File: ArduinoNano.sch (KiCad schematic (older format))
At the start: 14 parts, among them IC801 ATMEGA328P-AU, IC802 FT232RL-TUBE, J801 M20-9980345, J802 USB_Connector, Y801 Crystal

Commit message: finalized nano (references, one more resistor...)
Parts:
- removed R199: 146, symbol Device:R
- added RP1D801, RP2C801: 1k, symbol Device:R
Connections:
- net +5V: now also RP1D801.1
- net GND: now also RP2C801.1, RP2C801.2
- net RESET: now also IC801.29 (PC6_[RESET/PCINT14]), RP1D801.2
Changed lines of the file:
@@
 U 1 1 60D08921
 P 2850 1900
-F 0 "RP1B801" H 2600 2050 50  0000 L CNN
+F 0 "RP1B801" H 2500 2050 50  0000 L CNN
 F 1 "1k" H 2600 1950 50  0000 L CNN
 F 2 "" V 2780 1900 50  0001 C CNN
@@
 U 1 1 60D0986A
 P 3100 1900
-F 0 "RP1A801" H 3100 2050 50  0000 L CNN
-F 1 "1k" H 3200 1950 50  0000 L CNN
+F 0 "RP1A801" H 2750 2150 50  0000 L CNN
+F 1 "1k" H 2950 2050 50  0000 L CNN
 F 2 "" V 3030 1900 50  0001 C CNN
 F 3 "~" H 3100 1900 50  0001 C CNN
@@
 U 1 1 60D5814C
 P 1200 5200
-F 0 "C803" H 1315 5246 50  0000 L CNN
-F 1 "1uf" H 1315 5155 50  0000 L CNN
+F 0 "C803" H 900 5300 50  0000 L CNN
+F 1 "1uf" H 950 5200 50  0000 L CNN
 F 2 "" H 1238 5050 50  0001 C CNN
 F 3 "~" H 1200 5200 50  0001 C CNN
@@
 U 1 1 60D58539
 P 1900 5200
-F 0 "C805" H 2015 5246 50  0000 L CNN
+F 0 "C805" H 2000 5250 50  0000 L CNN
 F 1 "1uf" H 2015 5155 50  0000 L CNN
 F 2 "" H 1938 5050 50  0001 C CNN
@@
 U 1 1 60D58EE5
 P 1550 5200
-F 0 "C804" H 1668 5246 50  0000 L CNN
-F 1 "4.7uF_16V" H 1450 5350 50  0000 L CNN
+F 0 "C804" H 1350 5100 50  0000 L CNN
+F 1 "4.7uF_16V" H 1350 5000 50  0000 L CNN
 F 2 "" H 1588 5050 50  0001 C CNN
 F 3 "~" H 1550 5200 50  0001 C CNN
@@
 U 1 1 60D9EF9C
 P 1050 4100
-F 0 "C801" V 900 4100 50  0000 C CNN
+F 0 "C801" V 900 4050 50  0000 C CNN
 F 1 "C" V 900 4200 50  0000 C CNN
 F 2 "" H 1088 3950 50  0001 C CNN
@@
 U 1 1 60DA0A1E
 P 1050 4400
-F 0 "C802" V 1200 4400 50  0000 C CNN
+F 0 "C802" V 1200 4350 50  0000 C CNN
 F 1 "C" V 1200 4500 50  0000 C CNN
 F 2 "" H 1088 4250 50  0001 C CNN
@@
 Wire Wire Line
 	6200 5800 5650 5800
-$Comp
-L Device:R R199
-U 1 1 60CC8A37
-P 7200 2300
-F 0 "R199" H 7270 2346 50  0000 L CNN
-F 1 "146" H 7270 2255 50  0000 L CNN
-F 2 "" V 7130 2300 50  0001 C CNN
-F 3 "~" H 7200 2300 50  0001 C CNN
-	1    7200 2300
-	1    0    0    -1
-$EndComp
+Wire Wire Line
+	3350 1800 3350 2200
+Wire Wire Line
+	3350 1800 3850 1800
+Wire Wire Line
+	3850 1800 3850 1700
+$Comp
+L Device:R RP1D801
+U 1 1 60CE678B
+P 3850 1550
+F 0 "RP1D801" H 3920 1596 50  0000 L CNN
+F 1 "1k" H 3920 1505 50  0000 L CNN
+F 2 "" V 3780 1550 50  0001 C CNN
+F 3 "~" H 3850 1550 50  0001 C CNN
+	1    3850 1550
+	1    0    0    -1
+$EndComp
+$Comp
+L power:+5V #PWR0813
+U 1 1 60CE727D
+P 3850 1400
+F 0 "#PWR0813" H 3850 1250 50  0001 C CNN
+F 1 "+5V" H 3865 1573 50  0000 C CNN
+F 2 "" H 3850 1400 50  0001 C CNN
+F 3 "" H 3850 1400 50  0001 C CNN
+	1    3850 1400
+	1    0    0    -1
+$EndComp
+Text Label 3450 1800 0    50   ~ 0
+RESET
+$Comp
+L Device:R RP2C801
+U 1 1 60CEA708
+P 5550 3100
+F 0 "RP2C801" V 5343 3100 50  0000 C CNN
+F 1 "1k" V 5434 3100 50  0000 C CNN
+F 2 "" V 5480 3100 50  0001 C CNN
+F 3 "~" H 5550 3100 50  0001 C CNN
+	1    5550 3100
+	0    1    1    0
+$EndComp
+Wire Wire Line
+	5700 3100 5700 3250
+Wire Wire Line
+	5700 3250 5400 3250
+Wire Wire Line
+	5400 3250 5400 3100
+Wire Wire Line
+	5400 3250 5400 3350
+Connection ~ 5400 3250
+$Comp
+L power:GND #PWR0814
+U 1 1 60CF0B8E
+P 5400 3350
+F 0 "#PWR0814" H 5400 3100 50  0001 C CNN
+F 1 "GND" H 5405 3177 50  0000 C CNN
+F 2 "" H 5400 3350 50  0001 C CNN
+F 3 "" H 5400 3350 50  0001 C CNN
+	1    5400 3350
+	1    0    0    -1
+$EndComp

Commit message: add footprints julia
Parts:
- IC802: footprint SOP65P780X200-28N -> footprint libraries:FT232RL-TUBE
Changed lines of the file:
@@
 F 0 "IC802" H 8500 4315 50  0000 C CNN
 F 1 "FT232RL-TUBE" H 8500 4224 50  0000 C CNN
-F 2 "SOP65P780X200-28N" H 9000 4150 50  0001 L CNN
+F 2 "footprint libraries:FT232RL-TUBE" H 9000 4150 50  0001 L CNN
 F 3 "http://www.ftdichip.com/Support/Documents/DataSheets/ICs/DS_FT232R.pdf" H 9000 4050 50  0001 L CNN
 F 4 "USB Interface IC FT232R Single Ch Full Speed" H 9000 3950 50  0001 L CNN "Description"

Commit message: add footprints 2 julia
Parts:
- IC801: footprint QFP80P900X900X120-32N -> footprint libraries:QFP80P900X900X120-32N
- J801: footprint HDRV6W64P254_2X3_762X508X864P -> footprint libraries:M20-9980345
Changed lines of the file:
@@
 F 0 "IC801" H 3400 3300 50  0000 L CNN
 F 1 "ATMEGA328P-AU" H 3150 3200 50  0000 L CNN
-F 2 "QFP80P900X900X120-32N" H 4300 4800 50  0001 L CNN
+F 2 "footprint libraries:QFP80P900X900X120-32N" H 4300 4800 50  0001 L CNN
 F 3 "https://componentsearchengine.com/Datasheets/2/ATMEGA328P-AU.pdf" H 4300 4700 50  0001 L CNN
 F 4 "MICROCHIP - ATMEGA328P-AU. - MICROCONTROLLER MCU, 8 BIT, ATMEGA, 20MHZ, TQFP-32" H 4300 4600 50  0001 L CNN "Description"
@@
 F 0 "J801" H 6600 5865 50  0000 C CNN
 F 1 "M20-9980345" H 6600 5774 50  0000 C CNN
-F 2 "HDRV6W64P254_2X3_762X508X864P" H 6850 5700 50  0001 L CNN
+F 2 "footprint libraries:M20-9980345" H 6850 5700 50  0001 L CNN
 F 3 "https://componentsearchengine.com/Datasheets/2/M20-9980345.pdf" H 6850 5600 50  0001 L CNN
 F 4 "M20 Header, Pin, Dil, Vertical, 3+3 W HARWIN M20 Series, 2.54mm Pitch 6 Way 2 Row Straight Pin Header, Through Hole, Solder Termination" H 6850 5500 50  0001 L CNN "Description"

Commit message: added vishay dude & capacitor & resistor footprints
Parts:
- C801, C802, C803, C804, C805, C806: footprint (none) -> Capacitor_SMD:C_0402_1005Metric
- J802: footprint (none) -> footprint libraries:UX60MB5ST
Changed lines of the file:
@@
 F 0 "C806" H 5315 4346 50  0000 L CNN
 F 1 "100nF" H 5315 4255 50  0000 L CNN
-F 2 "" H 5238 4150 50  0001 C CNN
+F 2 "Capacitor_SMD:C_0402_1005Metric" H 5238 4150 50  0001 C CNN
 F 3 "~" H 5200 4300 50  0001 C CNN
 	1    5200 4300
@@
 F 0 "C803" H 900 5300 50  0000 L CNN
 F 1 "1uf" H 950 5200 50  0000 L CNN
-F 2 "" H 1238 5050 50  0001 C CNN
+F 2 "Capacitor_SMD:C_0402_1005Metric" H 1238 5050 50  0001 C CNN
 F 3 "~" H 1200 5200 50  0001 C CNN
 	1    1200 5200
@@
 F 0 "C805" H 2000 5250 50  0000 L CNN
 F 1 "1uf" H 2015 5155 50  0000 L CNN
-F 2 "" H 1938 5050 50  0001 C CNN
+F 2 "Capacitor_SMD:C_0402_1005Metric" H 1938 5050 50  0001 C CNN
 F 3 "~" H 1900 5200 50  0001 C CNN
 	1    1900 5200
@@
 F 0 "C804" H 1350 5100 50  0000 L CNN
 F 1 "4.7uF_16V" H 1350 5000 50  0000 L CNN
-F 2 "" H 1588 5050 50  0001 C CNN
+F 2 "Capacitor_SMD:C_0402_1005Metric" H 1588 5050 50  0001 C CNN
 F 3 "~" H 1550 5200 50  0001 C CNN
 	1    1550 5200
@@
 F 0 "C801" V 900 4050 50  0000 C CNN
 F 1 "C" V 900 4200 50  0000 C CNN
-F 2 "" H 1088 3950 50  0001 C CNN
+F 2 "Capacitor_SMD:C_0402_1005Metric" H 1088 3950 50  0001 C CNN
 F 3 "~" H 1050 4100 50  0001 C CNN
 	1    1050 4100
@@
 F 0 "C802" V 1200 4350 50  0000 C CNN
 F 1 "C" V 1200 4500 50  0000 C CNN
-F 2 "" H 1088 4250 50  0001 C CNN
+F 2 "Capacitor_SMD:C_0402_1005Metric" H 1088 4250 50  0001 C CNN
 F 3 "~" H 1050 4400 50  0001 C CNN
 	1    1050 4400
@@
 F 0 "J802" H 10400 5815 50  0000 C CNN
 F 1 "USB_Connector" H 10400 5724 50  0000 C CNN
-F 2 "" H 10400 5350 50  0001 C CNN
+F 2 "footprint libraries:UX60MB5ST" H 10400 5350 50  0001 C CNN
 F 3 "" H 10400 5350 50  0001 C CNN
 	1    10400 5350

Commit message: added osciallator libs
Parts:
- RP1A801, RP1B801, RP1D801, RP2C801: footprint (none) -> Resistor_SMD:R_0402_1005Metric
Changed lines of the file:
@@
 F 0 "RP1B801" H 2500 2050 50  0000 L CNN
 F 1 "1k" H 2600 1950 50  0000 L CNN
-F 2 "" V 2780 1900 50  0001 C CNN
+F 2 "Resistor_SMD:R_0402_1005Metric" V 2780 1900 50  0001 C CNN
 F 3 "~" H 2850 1900 50  0001 C CNN
 	1    2850 1900
@@
 F 0 "RP1A801" H 2750 2150 50  0000 L CNN
 F 1 "1k" H 2950 2050 50  0000 L CNN
-F 2 "" V 3030 1900 50  0001 C CNN
+F 2 "Resistor_SMD:R_0402_1005Metric" V 3030 1900 50  0001 C CNN
 F 3 "~" H 3100 1900 50  0001 C CNN
 	1    3100 1900
@@
 F 0 "RP1D801" H 3920 1596 50  0000 L CNN
 F 1 "1k" H 3920 1505 50  0000 L CNN
-F 2 "" V 3780 1550 50  0001 C CNN
+F 2 "Resistor_SMD:R_0402_1005Metric" V 3780 1550 50  0001 C CNN
 F 3 "~" H 3850 1550 50  0001 C CNN
 	1    3850 1550
@@
 F 0 "RP2C801" V 5343 3100 50  0000 C CNN
 F 1 "1k" V 5434 3100 50  0000 C CNN
-F 2 "" V 5480 3100 50  0001 C CNN
+F 2 "Resistor_SMD:R_0402_1005Metric" V 5480 3100 50  0001 C CNN
 F 3 "~" H 5550 3100 50  0001 C CNN
 	1    5550 3100

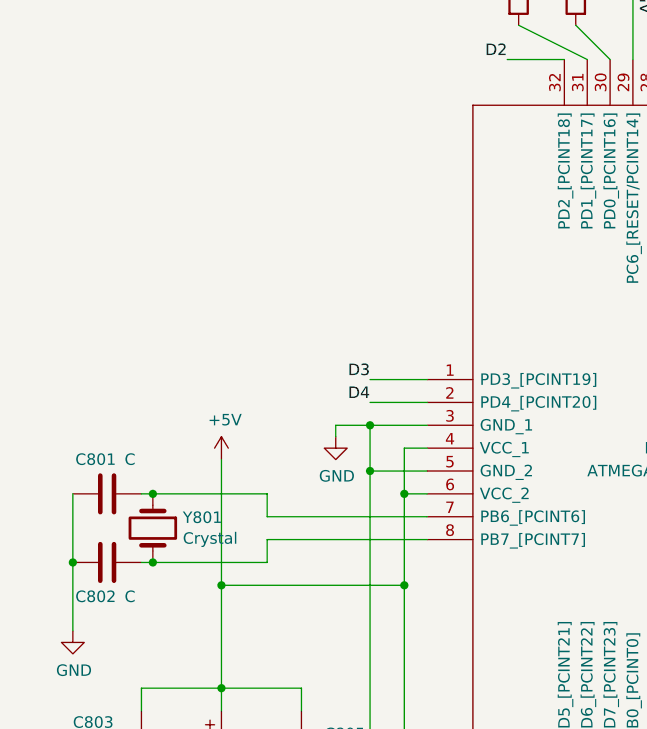
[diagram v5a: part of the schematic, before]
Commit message: replace crystal
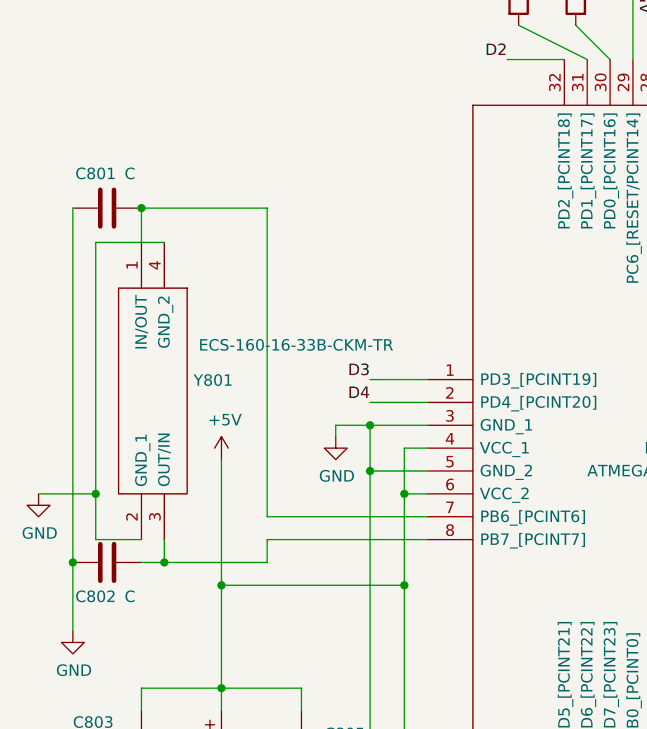
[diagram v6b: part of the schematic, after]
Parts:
- removed Y801: Crystal, symbol Device:Crystal
- added Y801: ECS-160-16-33B-CKM-TR, footprint libraries:ECS1601633BCKMTR, symbol ECS-160-16-33B-CKM-TR:ECS-160-16-33B-CKM-TR
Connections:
- net GND: now also Y801.2 (GND_1), Y801.4 (GND_2)
- net at C801.1, IC801.7 (PB6_[PCINT6]): now also Y801.1 (IN/OUT)
- net at C802.1, IC801.8 (PB7_[PCINT7]): now also Y801.3 (OUT/IN)
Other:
- moved on the sheet: C801
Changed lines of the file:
@@
 	1550 4500 1550 4950
 Connection ~ 1550 4500
-$Comp
-L Device:Crystal Y801
-U 1 1 60D95420
-P 1250 4250
-F 0 "Y801" V 1204 4381 50  0000 L CNN
-F 1 "Crystal" V 1295 4381 50  0000 L CNN
-F 2 "" H 1250 4250 50  0001 C CNN
-F 3 "~" H 1250 4250 50  0001 C CNN
-	1    1250 4250
-	0    1    1    0
-$EndComp
-Wire Wire Line
-	1750 4200 1750 4100
-Wire Wire Line
-	1750 4100 1250 4100
-Connection ~ 1250 4100
 Wire Wire Line
 	1750 4300 1750 4400
-Wire Wire Line
-	1750 4400 1250 4400
 $Comp
 L Device:C C801
 U 1 1 60D9EF9C
-P 1050 4100
-F 0 "C801" V 900 4050 50  0000 C CNN
-F 1 "C" V 900 4200 50  0000 C CNN
-F 2 "Capacitor_SMD:C_0402_1005Metric" H 1088 3950 50  0001 C CNN
-F 3 "~" H 1050 4100 50  0001 C CNN
-	1    1050 4100
-	0    1    1    0
-$EndComp
-Wire Wire Line
-	1250 4100 1200 4100
+P 1050 2850
+F 0 "C801" V 900 2800 50  0000 C CNN
+F 1 "C" V 900 2950 50  0000 C CNN
+F 2 "Capacitor_SMD:C_0402_1005Metric" H 1088 2700 50  0001 C CNN
+F 3 "~" H 1050 2850 50  0001 C CNN
+	1    1050 2850
+	0    1    1    0
+$EndComp
 $Comp
 L Device:C C802
@@
 	0    1    1    0
 $EndComp
-Connection ~ 1250 4400
-Wire Wire Line
-	1200 4400 1250 4400
-Wire Wire Line
-	900  4100 900  4400
 Connection ~ 900  4400
 Wire Wire Line
@@
 	1    0    0    -1
 $EndComp
+$Comp
+L ECS-160-16-33B-CKM-TR:ECS-160-16-33B-CKM-TR Y801
+U 1 1 60CE517B
+P 1300 3000
+F 0 "Y801" V 1904 3128 50  0000 L CNN
+F 1 "ECS-160-16-33B-CKM-TR" V 1750 3150 50  0000 L CNN
+F 2 "footprint libraries:ECS1601633BCKMTR" H 2450 3100 50  0001 L CNN
+F 3 "" H 2450 3000 50  0001 L CNN
+F 4 "Crystals CRYSTAL 16.000MHZ 16PF SMD,ECS-33B,+/-10ppm,+/-10ppm,60 Ohm,Fundamental,-20 C 70 C,4-SMD, No Lead (DFN, LCC),0.126\" L x 0.098\" W (3.20mm x 2.50mm),0.031\" (0.80mm)" H 2450 2900 50  0001 L CNN "Description"
+F 5 "0.8" H 2450 2800 50  0001 L CNN "Height"
+F 6 "520-160-16-33B-CKMTR" H 2450 2700 50  0001 L CNN "Mouser Part Number"
+F 7 "https://www.mouser.co.uk/ProductDetail/ECS/ECS-160-16-33B-CKM-TR/?qs=W%2FMpXkg%252BdQ6JQ%2Fy9oiIGzw%3D%3D" H 2450 2600 50  0001 L CNN "Mouser Price/Stock"
+F 8 "ECS" H 2450 2500 50  0001 L CNN "Manufacturer_Name"
+F 9 "ECS-160-16-33B-CKM-TR" H 2450 2400 50  0001 L CNN "Manufacturer_Part_Number"
+	1    1300 3000
+	0    1    1    0
+$EndComp
+Wire Wire Line
+	1200 2850 1750 2850
+Wire Wire Line
+	1200 4400 1300 4400
+Wire Wire Line
+	1200 3000 1200 2850
+Connection ~ 1200 2850
+Wire Wire Line
+	1300 4300 1300 4400
+Connection ~ 1300 4400
+Wire Wire Line
+	1300 4400 1750 4400
+Wire Wire Line
+	1200 4300 1000 4300
+Wire Wire Line
+	1000 4300 1000 4100
+Wire Wire Line
+	1000 3000 1300 3000
+Wire Wire Line
+	900  2850 900  4400
+Wire Wire Line
+	1750 2850 1750 4200
+$Comp
+L power:GND #PWR0101
+U 1 1 60D0BCAF
+P 750 4100
+F 0 "#PWR0101" H 750 3850 50  0001 C CNN
+F 1 "GND" H 755 3927 50  0000 C CNN
+F 2 "" H 750 4100 50  0001 C CNN
+F 3 "" H 750 4100 50  0001 C CNN
+	1    750  4100
+	1    0    0    -1
+$EndComp
+Wire Wire Line
+	1000 4100 750  4100
+Connection ~ 1000 4100
+Wire Wire Line
+	1000 4100 1000 3000
 $EndSCHEMATC

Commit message: changes on nano and laser
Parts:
- removed RP2C801: 1k, Resistor_SMD:R_0402_1005Metric, symbol Device:R
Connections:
- net D0-RX: now reaches IC801.30 (PD0_[PCINT16]), RP1A801.2
- net D1-TX: now reaches IC801.31 (PD1_[PCINT17]), RP1B801.2
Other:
- moved on the sheet: RP1A801, RP1B801
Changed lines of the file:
@@
 $EndComp
 Wire Wire Line
-	3150 2200 2850 2050
+	3150 2100 2350 2100
 $Comp
 L Device:R RP1B801
 U 1 1 60D08921
-P 2850 1900
-F 0 "RP1B801" H 2500 2050 50  0000 L CNN
-F 1 "1k" H 2600 1950 50  0000 L CNN
-F 2 "Resistor_SMD:R_0402_1005Metric" V 2780 1900 50  0001 C CNN
-F 3 "~" H 2850 1900 50  0001 C CNN
-	1    2850 1900
-	1    0    0    -1
-$EndComp
-Wire Wire Line
-	2850 1750 2850 1450
-Text Label 2850 1450 1    50   ~ 0
+P 2350 1750
+F 0 "RP1B801" H 2000 1900 50  0000 L CNN
+F 1 "1k" H 2100 1800 50  0000 L CNN
+F 2 "Resistor_SMD:R_0402_1005Metric" V 2280 1750 50  0001 C CNN
+F 3 "~" H 2350 1750 50  0001 C CNN
+	1    2350 1750
+	1    0    0    -1
+$EndComp
+Wire Wire Line
+	2350 1600 2350 1300
+Text Label 2350 1300 1    50   ~ 0
 TX
 Wire Wire Line
-	3250 2200 3100 2050
+	3250 2000 2600 2000
 $Comp
 L Device:R RP1A801
 U 1 1 60D0986A
-P 3100 1900
-F 0 "RP1A801" H 2750 2150 50  0000 L CNN
-F 1 "1k" H 2950 2050 50  0000 L CNN
-F 2 "Resistor_SMD:R_0402_1005Metric" V 3030 1900 50  0001 C CNN
-F 3 "~" H 3100 1900 50  0001 C CNN
-	1    3100 1900
+P 2600 1750
+F 0 "RP1A801" H 2250 2000 50  0000 L CNN
+F 1 "1k" H 2450 1900 50  0000 L CNN
+F 2 "Resistor_SMD:R_0402_1005Metric" V 2530 1750 50  0001 C CNN
+F 3 "~" H 2600 1750 50  0001 C CNN
+	1    2600 1750
 	-1   0    0    -1
 $EndComp
 Wire Wire Line
-	3100 1750 3100 1500
-Text Label 3100 1500 1    50   ~ 0
+	2600 1600 2600 1350
+Text Label 2600 1350 1    50   ~ 0
 RX
 Wire Wire Line
@@
 RESET
 $Comp
-L Device:R RP2C801
-U 1 1 60CEA708
-P 5550 3100
-F 0 "RP2C801" V 5343 3100 50  0000 C CNN
-F 1 "1k" V 5434 3100 50  0000 C CNN
-F 2 "Resistor_SMD:R_0402_1005Metric" V 5480 3100 50  0001 C CNN
-F 3 "~" H 5550 3100 50  0001 C CNN
-	1    5550 3100
-	0    1    1    0
-$EndComp
-Wire Wire Line
-	5700 3100 5700 3250
-Wire Wire Line
-	5700 3250 5400 3250
-Wire Wire Line
-	5400 3250 5400 3100
-Wire Wire Line
-	5400 3250 5400 3350
-Connection ~ 5400 3250
-$Comp
-L power:GND #PWR0814
-U 1 1 60CF0B8E
-P 5400 3350
-F 0 "#PWR0814" H 5400 3100 50  0001 C CNN
-F 1 "GND" H 5405 3177 50  0000 C CNN
-F 2 "" H 5400 3350 50  0001 C CNN
-F 3 "" H 5400 3350 50  0001 C CNN
-	1    5400 3350
-	1    0    0    -1
-$EndComp
-$Comp
 L ECS-160-16-33B-CKM-TR:ECS-160-16-33B-CKM-TR Y801
 U 1 1 60CE517B
@@
 Wire Wire Line
 	1000 4100 1000 3000
+Wire Wire Line
+	3250 2200 3250 2000
+Wire Wire Line
+	2600 2000 2600 1900
+Wire Wire Line
+	3150 2100 3150 2200
+Wire Wire Line
+	2350 2100 2350 1900
+Text Label 2650 2100 2    50   ~ 0
+D1-TX
+Text Label 2950 2000 2    50   ~ 0
+D0-RX
 $EndSCHEMATC

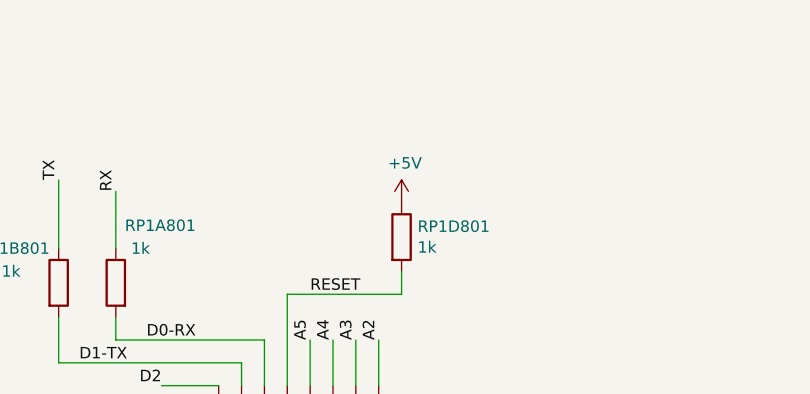
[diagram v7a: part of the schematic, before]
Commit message: add 5V label
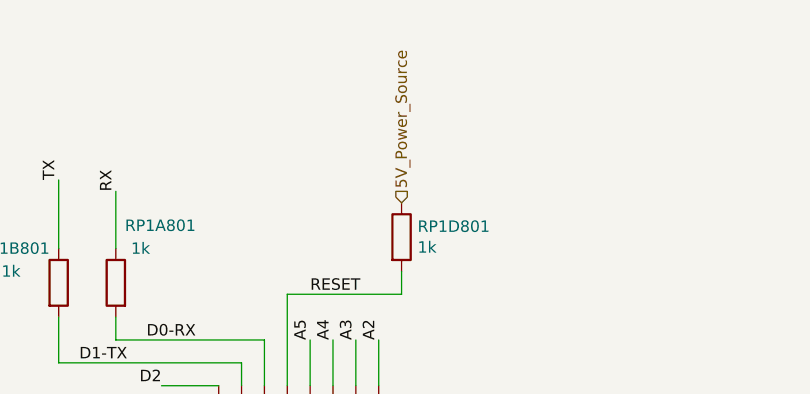
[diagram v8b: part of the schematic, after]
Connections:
- net +5V: no longer RP1D801.1
- new net 5V_Power_Source: RP1D801.1
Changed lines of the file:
@@
-	1    0    0    -1
-$EndComp
-$Comp
-L power:+5V #PWR0813
-U 1 1 60CE727D
-P 3850 1400
-F 0 "#PWR0813" H 3850 1250 50  0001 C CNN
-F 1 "+5V" H 3865 1573 50  0000 C CNN
-F 2 "" H 3850 1400 50  0001 C CNN
-F 3 "" H 3850 1400 50  0001 C CNN
-	1    3850 1400
 	1    0    0    -1
 $EndComp
@@
 Text Label 2950 2000 2    50   ~ 0
 D0-RX
+Text HLabel 3850 1400 1    50   Input ~ 0
+5V_Power_Source
 $EndSCHEMATC
